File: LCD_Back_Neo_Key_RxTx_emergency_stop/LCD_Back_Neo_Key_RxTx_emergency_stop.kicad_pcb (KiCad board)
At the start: 2 copper layers, 83.8 x 71.1 mm, 11 parts, among them J1 Screw_Terminal_01x09, J2 Conn_01x20_Female, J3 Conn_01x08_Male, J4 Conn_01x01_Female, J5 Conn_01x01_Female, Q1 BC337, U1 DC-DC_Stepdown-Zimprich

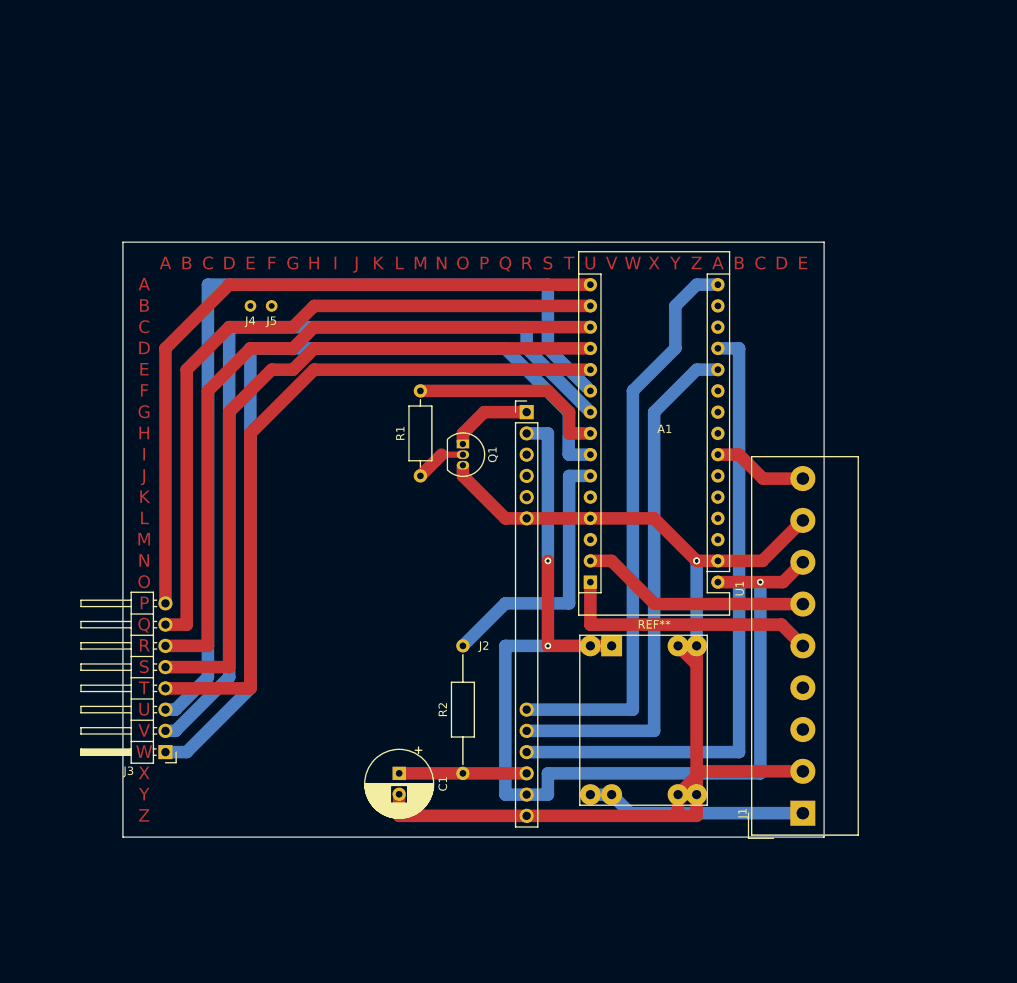
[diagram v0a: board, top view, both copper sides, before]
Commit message: add sheet for emergency stop
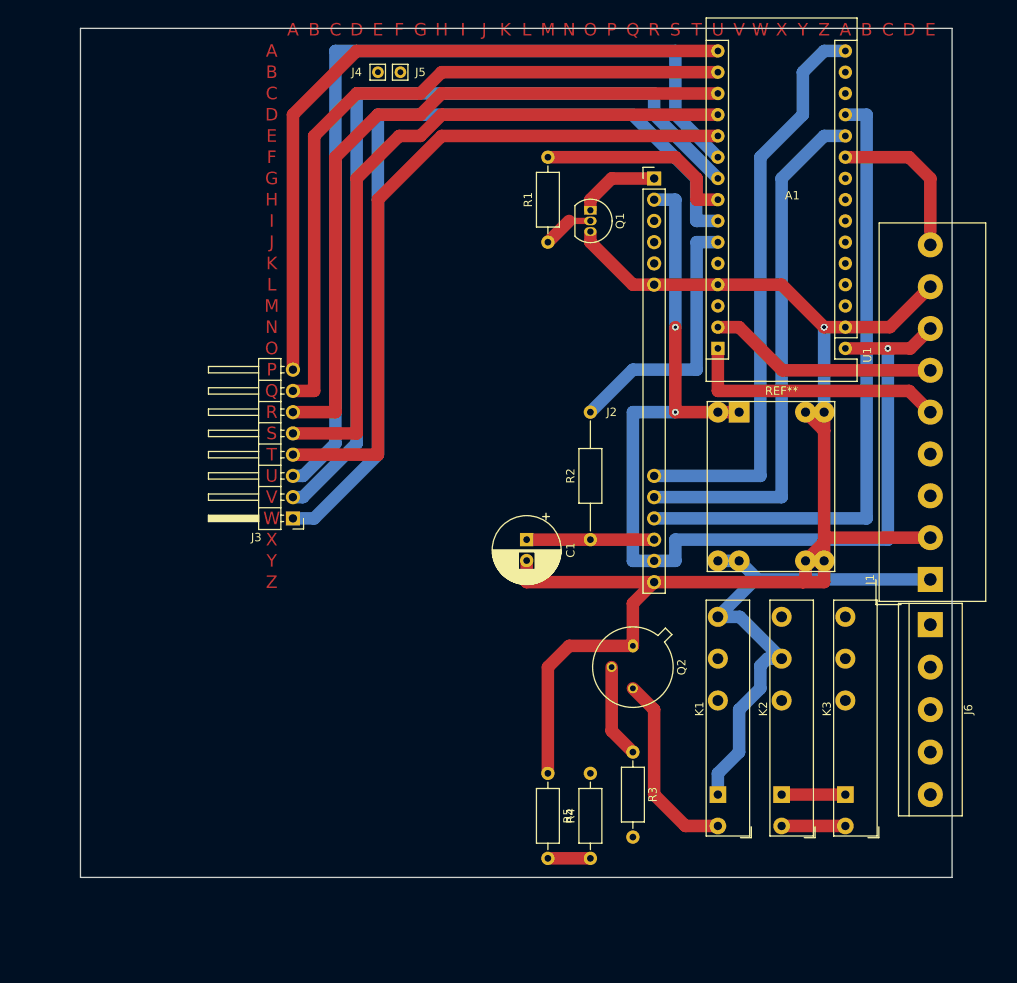
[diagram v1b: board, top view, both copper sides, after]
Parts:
- added J6: Screw_Terminal_01x05, TerminalBlock:TerminalBlock_bornier-5_P5.08mm, F.Cu at (205.7, 104.1)
- added K1: FINDER-34.51, Relay_THT:Relay_SPDT_Finder_34.51_Vertical, F.Cu at (180.3, 124.5)
- added K2: FINDER-34.51, Relay_THT:Relay_SPDT_Finder_34.51_Vertical, F.Cu at (188.0, 124.5)
- added K3: FINDER-34.51, Relay_THT:Relay_SPDT_Finder_34.51_Vertical, F.Cu at (195.6, 124.5)
- added Q2: 2N2222, Package_TO_SOT_THT:TO-39-3, F.Cu at (170.2, 106.7)
- added R3: 1k, Resistor_THT:R_Axial_DIN0207_L6.3mm_D2.5mm_P10.16mm_Horizontal, F.Cu at (170.2, 119.4)
- added R4: 100k, Resistor_THT:R_Axial_DIN0207_L6.3mm_D2.5mm_P10.16mm_Horizontal, F.Cu at (165.1, 132.1)
- added R5: 10k, Resistor_THT:R_Axial_DIN0207_L6.3mm_D2.5mm_P10.16mm_Horizontal, F.Cu at (160.0, 121.9)
- J3: value Conn_01x08_Male -> Conn_01x08_Male_KeyPad
- J4, J5: value Conn_01x01_Female -> Display_support_pin
- moved J5 31.9 mm to (142.4, 38.1)
- moved J1 31.8 mm to (205.7, 98.7)
- moved A1 31.8 mm to (188.0, 53.3)
- moved J2 31.8 mm to (172.7, 74.9)
- moved R1 31.8 mm to (160.0, 58.4)
- moved J3 31.8 mm to (129.5, 91.4)
- moved J4 31.8 mm to (139.7, 38.1)
- moved C1 31.8 mm to (157.5, 94.0)
- moved Q1 31.8 mm to (165.1, 54.6)
- moved R2 31.8 mm to (165.1, 94.0)
- moved U1 31.8 mm to (193.0, 76.2)
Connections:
- net Net-(A1-Pad23) renamed Ardu_A4
- net Net-(J1-Pad1) renamed VCC-24V
- A1 pad 21: Net-(A1-Pad21) -> Ardu_A2
- A1 pad 22: Net-(A1-Pad22) -> Ardu_A3
- A1 pad 25: Net-(A1-Pad25) -> Ardu_A6
- J1 pad 9: Ardu_A5 -> Ardu_A2
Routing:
- net VCC-24V: track 26.3 -> 63.0 mm
- net GND: track 140.8 -> 173.4 mm
- net Net-(K1-PadA2): track 0.00 -> 22.9 mm
- net Ardu_A2: track 0.00 -> 17.6 mm
- net Ardu_A5: track 11.3 -> 0.00 mm
- net Net-(Q2-Pad2): track 0.00 -> 11.2 mm
- net Net-(K1-Pad11): track 0.00 -> 7.62 mm
- net Net-(J6-Pad4): track 0.00 -> 7.62 mm
- net Ardu_A6: track 0.00 -> 5.08 mm
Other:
- board size 83.8 x 71.1 mm -> 104.2 x 101.5 mm

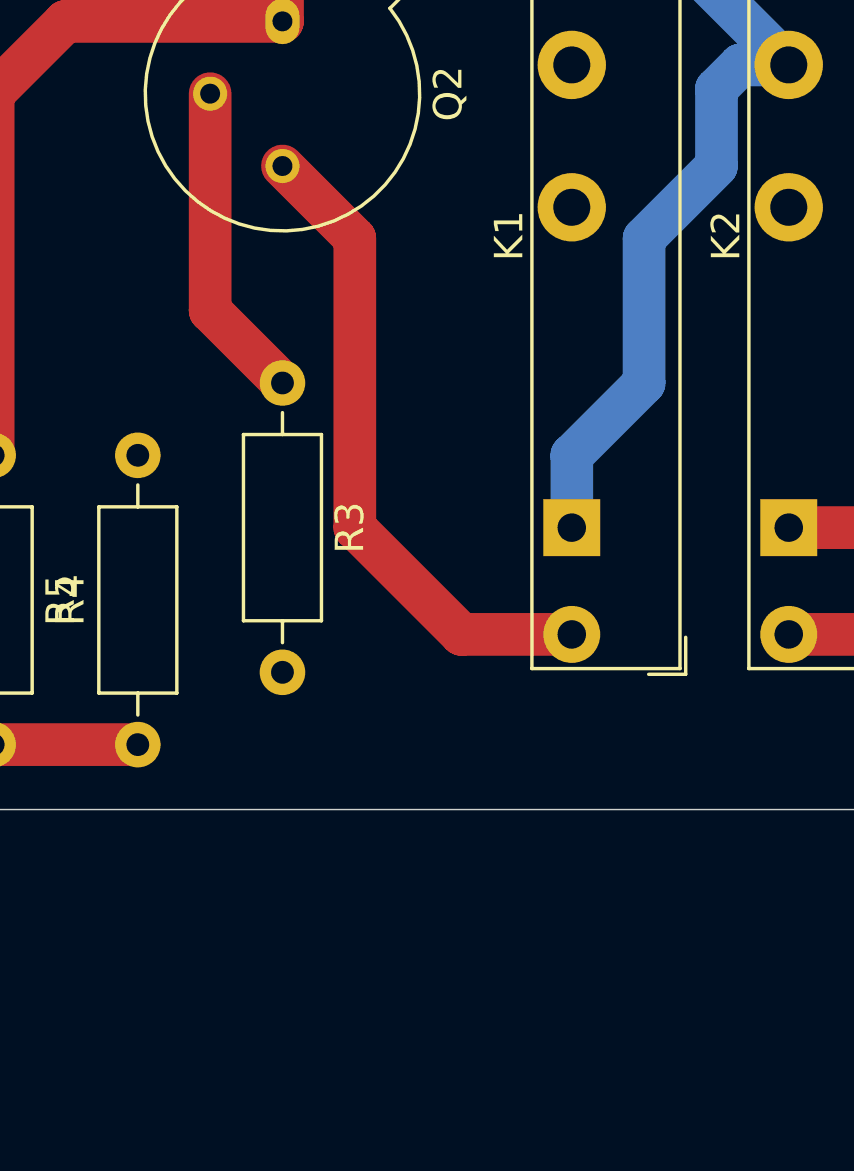
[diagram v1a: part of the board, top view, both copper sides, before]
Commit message: add freewheeling diode for relays
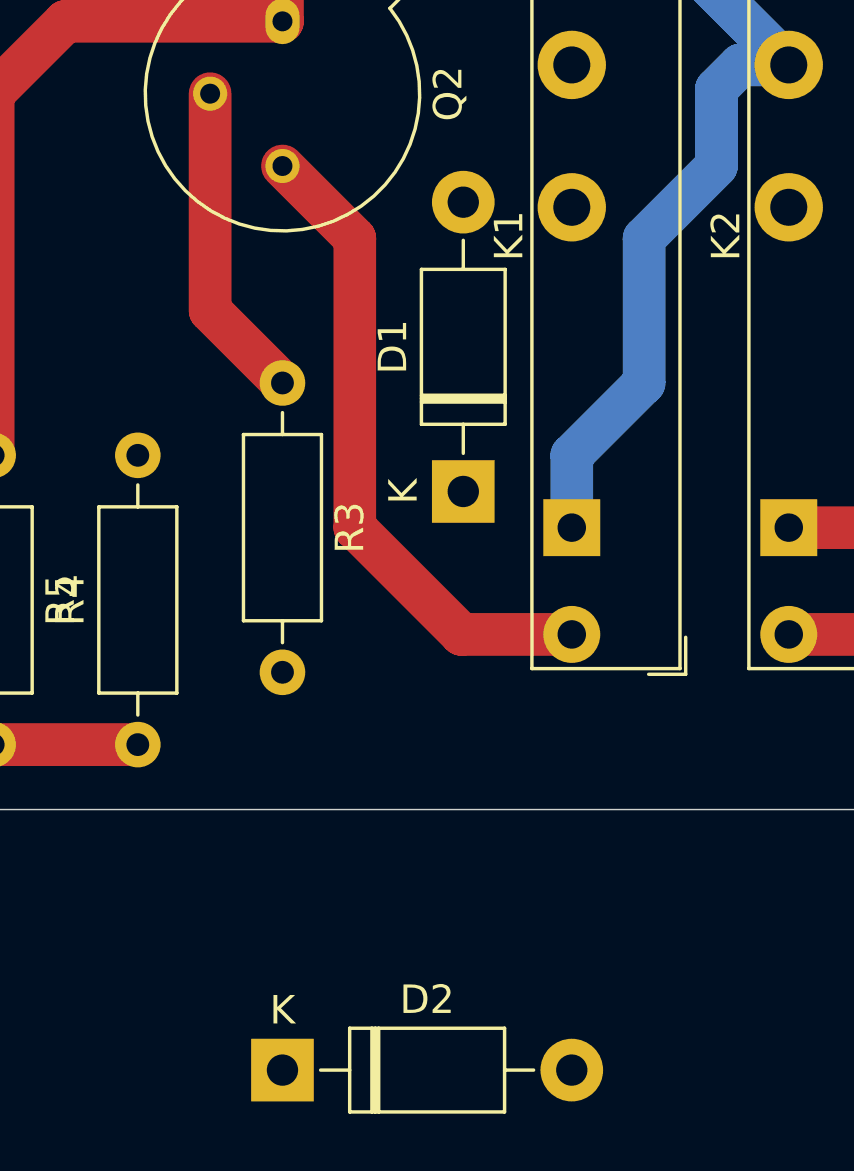
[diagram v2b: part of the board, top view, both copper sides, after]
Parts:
- added D1: 1N4004, Diode_THT:D_DO-41_SOD81_P10.16mm_Horizontal, F.Cu at (176.5, 123.2)
- added D2: 1N4004, Diode_THT:D_DO-41_SOD81_P10.16mm_Horizontal, F.Cu at (170.2, 143.5)

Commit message: remove ABCCDEF....
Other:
- board text removed: "A"
- board text removed: "B"
- board text removed: "C"
- board text removed: "D"
- board text removed: "E"
- board text removed: "F"
- board text removed: "G"
- board text removed: "H"
- board text removed: "I"
- board text removed: "J"
- board text removed: "K"
- board text removed: "L"
- board text removed: "M"
- board text removed: "N"
- board text removed: "O"
- board text removed: "P"
- board text removed: "Q"
- board text removed: "R"
- board text removed: "S"
- board text removed: "T"
- board text removed: "U"
- board text removed: "V"
- board text removed: "W"
- board text removed: "X"
- board text removed: "Y"
- board text removed: "Z"
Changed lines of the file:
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@@
-(kicad_pcb (version 20171130) (host pcbnew "(5.1.0-9-gc61ec8ee3)")
+(kicad_pcb (version 20171130) (host pcbnew "(5.1.0-13-ge6234d50d)")
   (general
     (thickness 1.6)
-    (drawings 61)
+    (drawings 4)
     (tracks 161)
     (zones 0)
@@
   (gr_line (start 208.34 32.86) (end 208.34 134.36) (layer Edge.Cuts) (width 0.05))
   (gr_line (start 104.14 134.36) (end 208.34 134.36) (layer Edge.Cuts) (width 0.05))
-  (gr_text C (at 200.66 33.02) (layer F.Cu)
-    (effects (font (size 1.5 1.5) (thickness 0.3)))
-  )
-  (gr_text D (at 203.2 33.02) (layer F.Cu)
-    (effects (font (size 1.5 1.5) (thickness 0.3)))
-  )
-  (gr_text B (at 198.12 33.02) (layer F.Cu)
-    (effects (font (size 1.5 1.5) (thickness 0.3)))
-  )
-  (gr_text A (at 195.58 33.02) (layer F.Cu)
-    (effects (font (size 1.5 1.5) (thickness 0.3)))
-  )
-  (gr_text E (at 205.74 33.02) (layer F.Cu)
-    (effects (font (size 1.5 1.5) (thickness 0.3)))
-  )
-  (gr_text N (at 162.56 33.02) (layer F.Cu)
-    (effects (font (size 1.5 1.5) (thickness 0.3)))
-  )
-  (gr_text M (at 160.02 33.02) (layer F.Cu)
-    (effects (font (size 1.5 1.5) (thickness 0.3)))
-  )
-  (gr_text Z (at 193.04 33.02) (layer F.Cu)
-    (effects (font (size 1.5 1.5) (thickness 0.3)))
-  )
-  (gr_text Y (at 190.5 33.02) (layer F.Cu)
-    (effects (font (size 1.5 1.5) (thickness 0.3)))
-  )
-  (gr_text X (at 187.96 33.02) (layer F.Cu)
-    (effects (font (size 1.5 1.5) (thickness 0.3)))
-  )
-  (gr_text W (at 185.42 33.02) (layer F.Cu)
-    (effects (font (size 1.5 1.5) (thickness 0.3)))
-  )
-  (gr_text V (at 182.88 33.02) (layer F.Cu)
-    (effects (font (size 1.5 1.5) (thickness 0.3)))
-  )
-  (gr_text U (at 180.34 33.02) (layer F.Cu)
-    (effects (font (size 1.5 1.5) (thickness 0.3)))
-  )
-  (gr_text T (at 177.8 33.02) (layer F.Cu)
-    (effects (font (size 1.5 1.5) (thickness 0.3)))
-  )
-  (gr_text S (at 175.26 33.02) (layer F.Cu)
-    (effects (font (size 1.5 1.5) (thickness 0.3)))
-  )
-  (gr_text R (at 172.72 33.02) (layer F.Cu)
-    (effects (font (size 1.5 1.5) (thickness 0.3)))
-  )
-  (gr_text Q (at 170.18 33.02) (layer F.Cu)
-    (effects (font (size 1.5 1.5) (thickness 0.3)))
-  )
-  (gr_text P (at 167.64 33.02) (layer F.Cu)
-    (effects (font (size 1.5 1.5) (thickness 0.3)))
-  )
-  (gr_text O (at 165.1 33.02) (layer F.Cu)
-    (effects (font (size 1.5 1.5) (thickness 0.3)))
-  )
-  (gr_text L (at 157.48 33.02) (layer F.Cu)
-    (effects (font (size 1.5 1.5) (thickness 0.3)))
-  )
-  (gr_text K (at 154.94 33.02) (layer F.Cu)
-    (effects (font (size 1.5 1.5) (thickness 0.3)))
-  )
-  (gr_text I (at 149.86 33.02) (layer F.Cu)
-    (effects (font (size 1.5 1.5) (thickness 0.3)))
-  )
-  (gr_text J (at 152.4 33.02) (layer F.Cu)
-    (effects (font (size 1.5 1.5) (thickness 0.3)))
-  )
-  (gr_text H (at 147.32 33.02) (layer F.Cu)
-    (effects (font (size 1.5 1.5) (thickness 0.3)))
-  )
-  (gr_text G (at 144.78 33.02) (layer F.Cu)
-    (effects (font (size 1.5 1.5) (thickness 0.3)))
-  )
-  (gr_text F (at 142.24 33.02) (layer F.Cu)
-    (effects (font (size 1.5 1.5) (thickness 0.3)))
-  )
-  (gr_text E (at 139.7 33.02) (layer F.Cu)
-    (effects (font (size 1.5 1.5) (thickness 0.3)))
-  )
-  (gr_text D (at 137.16 33.02) (layer F.Cu)
-    (effects (font (size 1.5 1.5) (thickness 0.3)))
-  )
-  (gr_text C (at 134.62 33.02) (layer F.Cu)
-    (effects (font (size 1.5 1.5) (thickness 0.3)))
-  )
-  (gr_text B (at 132.08 33.02) (layer F.Cu)
-    (effects (font (size 1.5 1.5) (thickness 0.3)))
-  )
-  (gr_text A (at 129.54 33.02) (layer F.Cu)
-    (effects (font (size 1.5 1.5) (thickness 0.3)))
-  )
-  (gr_text A (at 127 35.56) (layer F.Cu)
-    (effects (font (size 1.5 1.5) (thickness 0.3)))
-  )
-  (gr_text B (at 127 38.1) (layer F.Cu)
-    (effects (font (size 1.5 1.5) (thickness 0.3)))
-  )
-  (gr_text C (at 127 40.64) (layer F.Cu)
-    (effects (font (size 1.5 1.5) (thickness 0.3)))
-  )
-  (gr_text D (at 127 43.18) (layer F.Cu)
-    (effects (font (size 1.5 1.5) (thickness 0.3)))
-  )
-  (gr_text E (at 127 45.72) (layer F.Cu)
-    (effects (font (size 1.5 1.5) (thickness 0.3)))
-  )
-  (gr_text F (at 127 48.26) (layer F.Cu)
-    (effects (font (size 1.5 1.5) (thickness 0.3)))
-  )
-  (gr_text G (at 127 50.8) (layer F.Cu)
-    (effects (font (size 1.5 1.5) (thickness 0.3)))
-  )
-  (gr_text H (at 127 53.34) (layer F.Cu)
-    (effects (font (size 1.5 1.5) (thickness 0.3)))
-  )
-  (gr_text I (at 127 55.88) (layer F.Cu)
-    (effects (font (size 1.5 1.5) (thickness 0.3)))
-  )
-  (gr_text J (at 127 58.42) (layer F.Cu)
-    (effects (font (size 1.5 1.5) (thickness 0.3)))
-  )
-  (gr_text K (at 127 60.96) (layer F.Cu)
-    (effects (font (size 1.5 1.5) (thickness 0.3)))
-  )
-  (gr_text L (at 127 63.5) (layer F.Cu)
-    (effects (font (size 1.5 1.5) (thickness 0.3)))
-  )
-  (gr_text M (at 127 66.04) (layer F.Cu)
-    (effects (font (size 1.5 1.5) (thickness 0.3)))
-  )
-  (gr_text N (at 127 68.58) (layer F.Cu)
-    (effects (font (size 1.5 1.5) (thickness 0.3)))
-  )
-  (gr_text O (at 127 71.12) (layer F.Cu)
-    (effects (font (size 1.5 1.5) (thickness 0.3)))
-  )
-  (gr_text P (at 127 73.66) (layer F.Cu)
-    (effects (font (size 1.5 1.5) (thickness 0.3)))
-  )
-  (gr_text Q (at 127 76.2) (layer F.Cu)
-    (effects (font (size 1.5 1.5) (thickness 0.3)))
-  )
-  (gr_text R (at 127 78.74) (layer F.Cu)
-    (effects (font (size 1.5 1.5) (thickness 0.3)))
-  )
-  (gr_text S (at 127 81.28) (layer F.Cu)
-    (effects (font (size 1.5 1.5) (thickness 0.3)))
-  )
-  (gr_text T (at 127 83.82) (layer F.Cu)
-    (effects (font (size 1.5 1.5) (thickness 0.3)))
-  )
-  (gr_text U (at 127 86.36) (layer F.Cu)
-    (effects (font (size 1.5 1.5) (thickness 0.3)))
-  )
-  (gr_text V (at 127 88.9) (layer F.Cu)
-    (effects (font (size 1.5 1.5) (thickness 0.3)))
-  )
-  (gr_text W (at 127 91.44) (layer F.Cu)
-    (effects (font (size 1.5 1.5) (thickness 0.3)))
-  )
-  (gr_text X (at 127 93.98) (layer F.Cu)
-    (effects (font (size 1.5 1.5) (thickness 0.3)))
-  )
-  (gr_text Y (at 127 96.52) (layer F.Cu)
-    (effects (font (size 1.5 1.5) (thickness 0.3)))
-  )
-  (gr_text Z (at 127 99.06) (layer F.Cu)
-    (effects (font (size 1.5 1.5) (thickness 0.3)))
-  )
   (segment (start 180.34 76.2) (end 203.2 76.2) (width 1.5) (layer F.Cu) (net 1))
   (segment (start 203.2 76.2) (end 205.74 78.74) (width 1.5) (layer F.Cu) (net 1))
@@
   (segment (start 180.34 121.92) (end 180.34 124.46) (width 1.5) (layer B.Cu) (net 36))
   (segment (start 182.88 119.38) (end 180.34 121.92) (width 1.5) (layer B.Cu) (net 36))
-  (segment (start 187.96 124.46) (end 195.58 124.46) (width 1.5) (layer F.Cu) (net 48))
-  (segment (start 176.47 128.21) (end 180.34 128.21) (width 1.5) (layer F.Cu) (net 47))
-  (segment (start 172.72 124.46) (end 176.47 128.21) (width 1.5) (layer F.Cu) (net 47))
-  (segment (start 170.18 111.76) (end 172.72 114.3) (width 1.5) (layer F.Cu) (net 47))
-  (segment (start 172.72 114.3) (end 172.72 124.46) (width 1.5) (layer F.Cu) (net 47))
-  (segment (start 187.96 128.21) (end 195.58 128.21) (width 1.5) (layer F.Cu) (net 49))
   (segment (start 167.64 109.22) (end 167.64 116.84) (width 1.5) (layer F.Cu) (net 42))
   (segment (start 167.64 116.84) (end 170.18 119.38) (width 1.5) (layer F.Cu) (net 42))
@@
   (segment (start 205.74 50.8) (end 205.74 57.15) (width 1.5) (layer F.Cu) (net 43))
   (segment (start 160.02 132.08) (end 165.1 132.08) (width 1.5) (layer F.Cu) (net 46))
+  (segment (start 176.47 128.21) (end 180.34 128.21) (width 1.5) (layer F.Cu) (net 47))
+  (segment (start 172.72 124.46) (end 176.47 128.21) (width 1.5) (layer F.Cu) (net 47))
+  (segment (start 170.18 111.76) (end 172.72 114.3) (width 1.5) (layer F.Cu) (net 47))
+  (segment (start 172.72 114.3) (end 172.72 124.46) (width 1.5) (layer F.Cu) (net 47))
+  (segment (start 187.96 124.46) (end 195.58 124.46) (width 1.5) (layer F.Cu) (net 48))
+  (segment (start 187.96 128.21) (end 195.58 128.21) (width 1.5) (layer F.Cu) (net 49))
 )

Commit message: place screwterminal on PCB
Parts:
- removed J6: Screw_Terminal_01x05, TerminalBlock:TerminalBlock_bornier-5_P5.08mm
- added JP1: Jumper_lon-jumper_lon, Jumper:SolderJumper-2_P1.3mm_Open_Pad1.0x1.5mm, F.Cu at (207.7, 114.3)
- added JP2: Jumper_lon-jumper_lon, Jumper:SolderJumper-2_P1.3mm_Open_Pad1.0x1.5mm, F.Cu at (207.7, 120.7)
- added K4: FINDER-34.51, Relay_THT:Relay_SPDT_Finder_34.51_Vertical, F.Cu at (201.9, 128.3)
- J1: value Screw_Terminal_01x09 -> Screw_Terminal_01x14; footprint TerminalBlock_Altech:Altech_AK300_1x09_P5.00mm_45-Degree -> Connector_Phoenix_MSTB:PhoenixContact_MSTBVA_2,5_14-G_1x14_P5.00mm_Vertical
- moved J1 62.5 mm to (207.0, 36.3), turned to 270 degrees
- moved Q2 30.5 mm to (139.7, 106.7)
- moved D2 29.6 mm to (190.5, 121.9), turned to 270 degrees
- moved R5 25.4 mm to (134.6, 121.9)
- moved D1 13.7 mm to (163.8, 118.1), turned to 270 degrees
- moved R3 12.8 mm to (157.5, 118.1)
- moved K2 5.39 mm to (184.2, 128.3)
- moved R4 5.08 mm to (170.2, 132.1)
- moved K1 4.58 mm to (177.8, 128.3)
- moved K3 3.81 mm to (195.6, 128.3)
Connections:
- J1 pad 1: VCC-24V -> Ardu_A2
- J1 pad 2: GND -> Ardu_A4
- J1 pad 3: Net-(J1-Pad3) -> Ardu_A5
- J1 pad 4: Net-(J1-Pad4) -> GND
- J1 pad 5: Net-(A1-Pad1) -> VCC-5V
- J1 pad 6: Net-(A1-Pad2) -> ScrewTerm8-EmrgencyRelay12
- J1 pad 7: VCC-5V -> ScrewTerm9-EmrgencyRelay14
- J1 pad 8: GND -> ScrewTerm10-EmrgencyRelay11
- J1 pad 9: Ardu_A2 -> ScrewTerm11-EmergencyStopSwitch1
- K3 pad 11: Net-(J6-Pad3) -> ScrewTerm10-EmrgencyRelay11
- K3 pad 12: Net-(J6-Pad1) -> ScrewTerm8-EmrgencyRelay12
- K3 pad 14: Net-(J6-Pad2) -> ScrewTerm9-EmrgencyRelay14
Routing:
- net Ardu_A6: track 5.08 -> 126.9 mm
- net Ardu_A3: track 0.00 -> 101.6 mm
- net Net-(D2-Pad1): track 7.62 -> 57.7 mm
- net VCC-24V: track 63.0 -> 112.6 mm
- net Net-(D2-Pad2): track 7.62 -> 47.4 mm
- net Net-(D1-Pad2): track 22.9 -> 56.8 mm
- net Net-(A1-Pad1): track 31.5 -> 0.00 mm
- net Net-(A1-Pad2): track 27.5 -> 0.00 mm
- net VCC-5V: track 125.4 -> 100.4 mm, vias 3 -> 2
- net GND: track 173.4 -> 190.8 mm
- net Ardu_A4: track 0.00 -> 16.8 mm
- net Net-(Q2-Pad2): track 11.2 -> 27.7 mm
- net Ardu_A5: track 0.00 -> 15.4 mm
- net ScrewTerm11-EmergencyStopSwitch1: track 0.00 -> 14.8 mm
- net Ardu_A0: track 76.2 -> 66.1 mm, vias 0 -> 1
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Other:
- board size 104.2 x 101.5 mm -> 105.5 x 101.5 mm
